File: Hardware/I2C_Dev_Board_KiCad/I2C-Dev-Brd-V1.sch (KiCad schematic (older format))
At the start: 23 parts, among them K1 POTS, P1 PICKIT2, P10 CONN_8, P2 FTDI SERIAL, P3 CONN_2, P4 CONN_6, P5 CONN_6, P6 CONN_4, P7 CONN_2, P8 CONN_2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

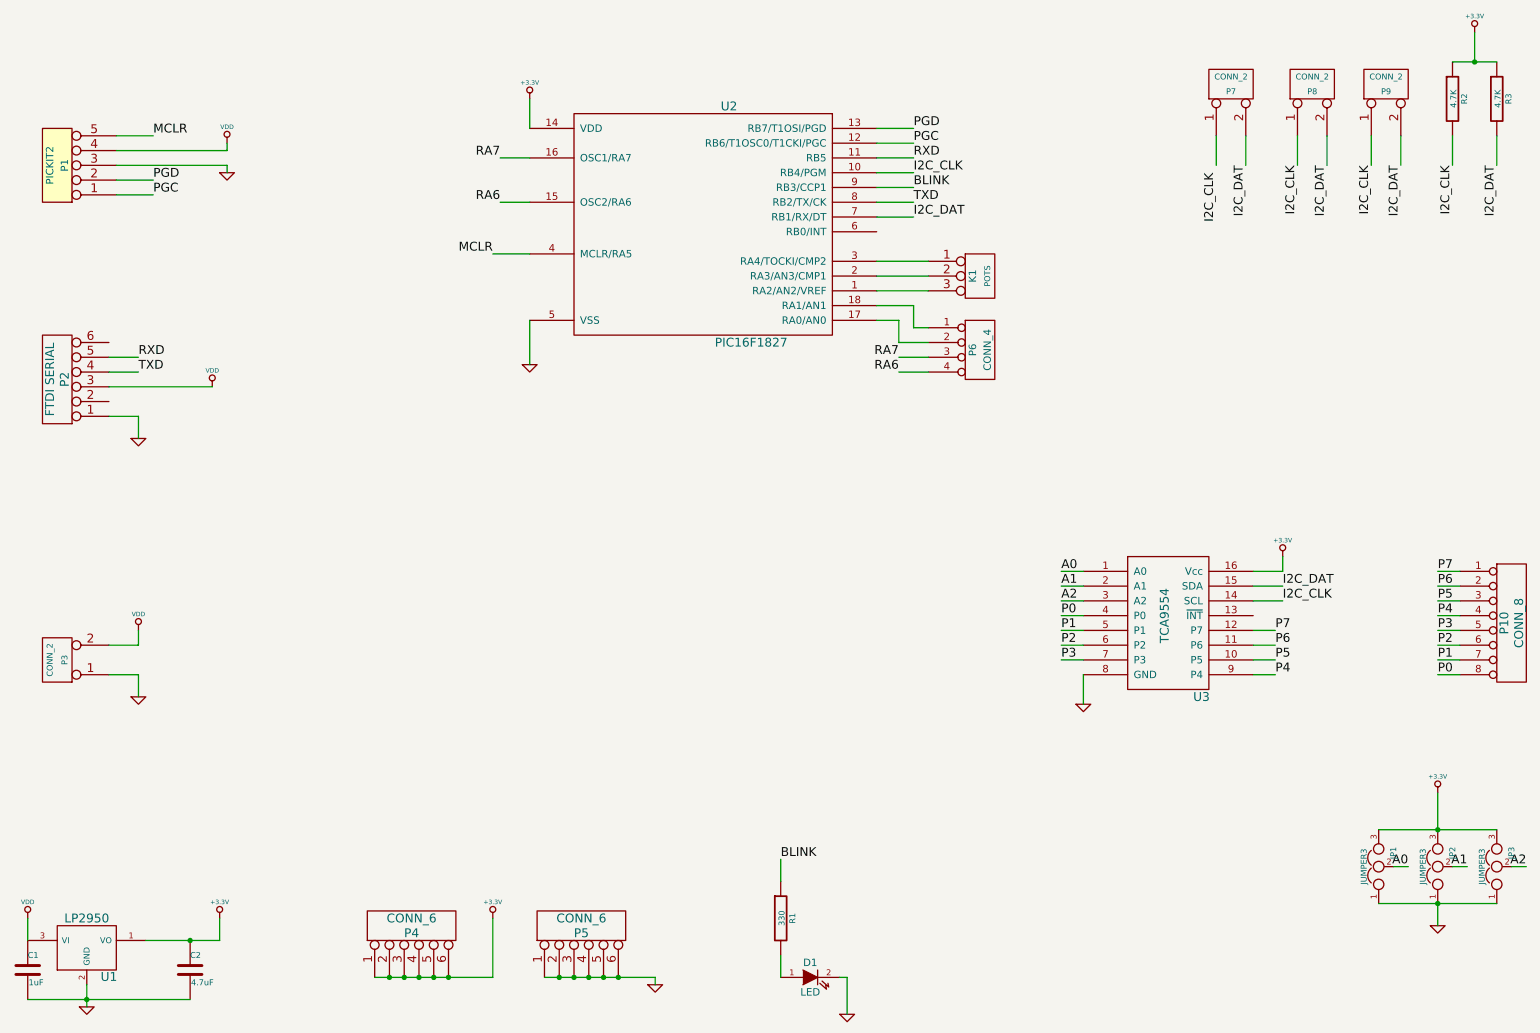
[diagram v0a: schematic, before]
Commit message: Added LUT table to firmware for VCO also added spreadsheet for LUT
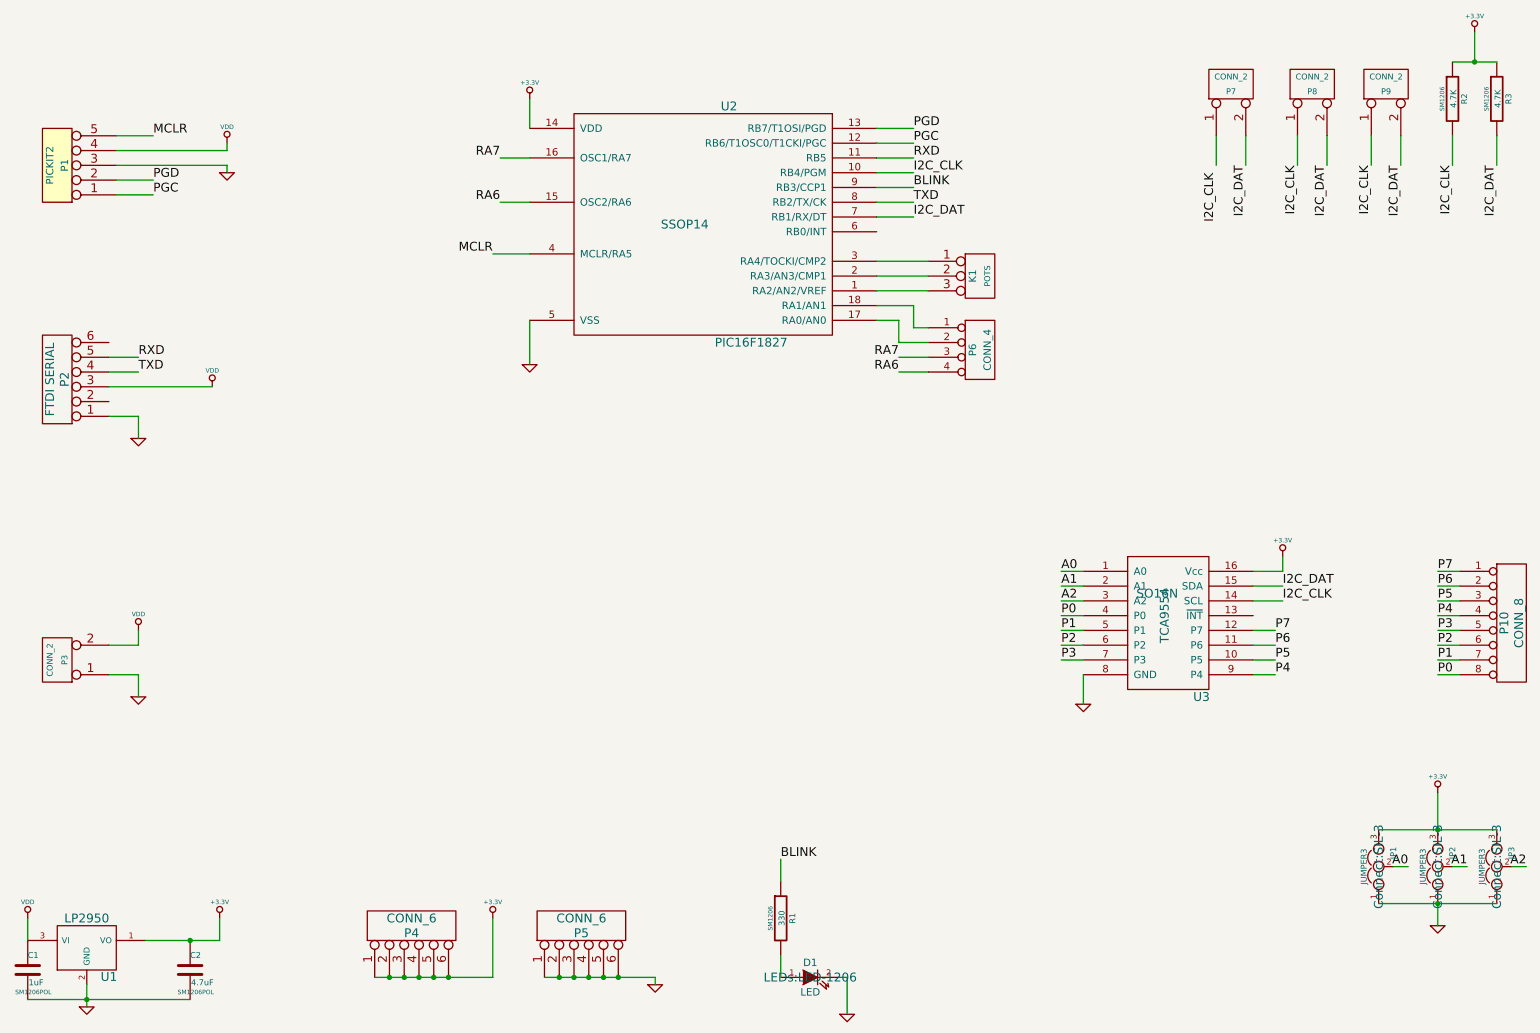
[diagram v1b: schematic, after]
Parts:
- C1, C2: footprint ~ -> SM1206POL
- D1: footprint ~ -> LEDs:LED-1206
- JP1, JP2, JP3: footprint ~ -> Connect:SIL-3
- K1: footprint (none) -> Connect:SIL-3
- P1: footprint (none) -> Connect:SIL-5
- P10: footprint (none) -> Connect:SIL-8
- P2, P4, P5: footprint (none) -> Connect:SIL-6
- P3, P7, P8, P9: footprint (none) -> Connect:SIL-2
- P6: footprint (none) -> Connect:SIL-4
- R1, R2, R3: footprint ~ -> SM1206
- U1: footprint (none) -> TO263
- U2: footprint ~ -> SSOP14
- U3: footprint ~ -> SO16N
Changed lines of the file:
@@
 LIBS:I2C
 LIBS:I2C-Dev-Brd-V1-cache
-EELAYER 27 0
+EELAYER 25 0
 EELAYER END
 $Descr A4 11693 8268
@@
 F 0 "U2" H 5600 2950 60  0000 C CNN
 F 1 "PIC16F1827" H 5750 1350 60  0000 C CNN
-F 2 "~" H 5300 2150 60  0000 C CNN
+F 2 "SSOP14" H 5300 2150 60  0000 C CNN
 F 3 "~" H 5300 2150 60  0000 C CNN
 	1    5300 2150
@@
 F 0 "P7" V 8950 1200 40  0000 C CNN
 F 1 "CONN_2" V 9050 1200 40  0000 C CNN
-F 2 "" H 9000 1200 60  0000 C CNN
+F 2 "Connect:SIL-2" H 9000 1200 60  0001 C CNN
 F 3 "" H 9000 1200 60  0000 C CNN
 	1    9000 1200
@@
 F 0 "P8" V 9500 1200 40  0000 C CNN
 F 1 "CONN_2" V 9600 1200 40  0000 C CNN
-F 2 "" H 9550 1200 60  0000 C CNN
+F 2 "Connect:SIL-2" H 9550 1200 60  0001 C CNN
 F 3 "" H 9550 1200 60  0000 C CNN
 	1    9550 1200
@@
 F 0 "P9" V 10000 1200 40  0000 C CNN
 F 1 "CONN_2" V 10100 1200 40  0000 C CNN
-F 2 "" H 10050 1200 60  0000 C CNN
+F 2 "Connect:SIL-2" H 10050 1200 60  0001 C CNN
 F 3 "" H 10050 1200 60  0000 C CNN
 	1    10050 1200
@@
 F 0 "R2" V 10580 1300 40  0000 C CNN
 F 1 "4.7K" V 10507 1301 40  0000 C CNN
-F 2 "~" V 10430 1300 30  0000 C CNN
+F 2 "SM1206" V 10430 1300 30  0000 C CNN
 F 3 "~" H 10500 1300 30  0000 C CNN
 	1    10500 1300
@@
 F 0 "R3" V 10880 1300 40  0000 C CNN
 F 1 "4.7K" V 10807 1301 40  0000 C CNN
-F 2 "~" V 10730 1300 30  0000 C CNN
+F 2 "SM1206" V 10730 1300 30  0000 C CNN
 F 3 "~" H 10800 1300 30  0000 C CNN
 	1    10800 1300
@@
 F 0 "P2" V 1000 3200 60  0000 C CNN
 F 1 "FTDI SERIAL" V 1100 3200 60  0000 C CNN
-F 2 "" H 1050 3200 60  0000 C CNN
+F 2 "Connect:SIL-6" H 1050 3200 60  0001 C CNN
 F 3 "" H 1050 3200 60  0000 C CNN
 	1    1050 3200
@@
 F 0 "D1" H 6150 7350 50  0000 C CNN
 F 1 "LED" H 6150 7150 50  0000 C CNN
-F 2 "~" H 6150 7250 60  0000 C CNN
+F 2 "LEDs:LED-1206" H 6150 7250 60  0000 C CNN
 F 3 "~" H 6150 7250 60  0000 C CNN
 	1    6150 7250
@@
 F 0 "R1" V 6030 6850 40  0000 C CNN
 F 1 "330" V 5957 6851 40  0000 C CNN
-F 2 "~" V 5880 6850 30  0000 C CNN
+F 2 "SM1206" V 5880 6850 30  0000 C CNN
 F 3 "~" H 5950 6850 30  0000 C CNN
 	1    5950 6850
@@
 F 0 "U1" H 1400 6854 60  0000 C CNN
 F 1 "LP2950" H 1250 7250 60  0000 C CNN
-F 2 "" H 1250 7050 60  0000 C CNN
+F 2 "TO263" H 1250 7050 60  0001 C CNN
 F 3 "" H 1250 7050 60  0000 C CNN
 	1    1250 7050
@@
 F 0 "C2" H 1950 7300 40  0000 L CNN
 F 1 "4.7uF" H 1956 7115 40  0000 L CNN
-F 2 "~" H 1988 7050 30  0000 C CNN
+F 2 "SM1206POL" H 1988 7050 30  0000 C CNN
 F 3 "~" H 1950 7200 60  0000 C CNN
 	1    1950 7200
@@
 F 0 "P1" V 1000 1750 50  0000 C CNN
 F 1 "PICKIT2" V 1100 1750 50  0000 C CNN
-F 2 "" H 1050 1750 60  0000 C CNN
+F 2 "Connect:SIL-5" H 1050 1750 60  0001 C CNN
 F 3 "" H 1050 1750 60  0000 C CNN
 	1    1050 1750
@@
 F 0 "P3" V 1000 5100 40  0000 C CNN
 F 1 "CONN_2" V 1100 5100 40  0000 C CNN
-F 2 "" H 1050 5100 60  0000 C CNN
+F 2 "Connect:SIL-2" H 1050 5100 60  0001 C CNN
 F 3 "" H 1050 5100 60  0000 C CNN
 	1    1050 5100
@@
 F 0 "K1" V 7250 2500 50  0000 C CNN
 F 1 "POTS" V 7350 2500 40  0000 C CNN
-F 2 "" H 7300 2500 60  0000 C CNN
+F 2 "Connect:SIL-3" H 7300 2500 60  0001 C CNN
 F 3 "" H 7300 2500 60  0000 C CNN
 	1    7300 2500
@@
 F 0 "P4" V 3400 6900 60  0000 C CNN
 F 1 "CONN_6" V 3500 6900 60  0000 C CNN
-F 2 "" H 3450 6900 60  0000 C CNN
+F 2 "Connect:SIL-6" H 3450 6900 60  0001 C CNN
 F 3 "" H 3450 6900 60  0000 C CNN
 	1    3450 6900
@@
 F 0 "P5" V 4550 6900 60  0000 C CNN
 F 1 "CONN_6" V 4650 6900 60  0000 C CNN
-F 2 "" H 4600 6900 60  0000 C CNN
+F 2 "Connect:SIL-6" H 4600 6900 60  0001 C CNN
 F 3 "" H 4600 6900 60  0000 C CNN
 	1    4600 6900
@@
 F 0 "P6" V 7250 3000 50  0000 C CNN
 F 1 "CONN_4" V 7350 3000 50  0000 C CNN
-F 2 "" H 7300 3000 60  0000 C CNN
+F 2 "Connect:SIL-4" H 7300 3000 60  0001 C CNN
 F 3 "" H 7300 3000 60  0000 C CNN
 	1    7300 3000
@@
 F 0 "U3" H 8800 4350 60  0000 C CNN
 F 1 "TCA9554" V 8550 4900 60  0000 C CNN
-F 2 "~" H 8500 5050 60  0000 C CNN
+F 2 "SO16N" H 8500 5050 60  0000 C CNN
 F 3 "~" H 8500 5050 60  0000 C CNN
 	1    8600 4850
@@
 F 0 "JP3" H 10850 6400 40  0000 L CNN
 F 1 "JUMPER3" H 10800 6600 40  0000 C CNN
-F 2 "~" H 10800 6500 60  0000 C CNN
+F 2 "Connect:SIL-3" H 10800 6500 60  0000 C CNN
 F 3 "~" H 10800 6500 60  0000 C CNN
 	1    10800 6500
@@
 F 0 "JP2" H 10450 6400 40  0000 L CNN
 F 1 "JUMPER3" H 10400 6600 40  0000 C CNN
-F 2 "~" H 10400 6500 60  0000 C CNN
+F 2 "Connect:SIL-3" H 10400 6500 60  0000 C CNN
 F 3 "~" H 10400 6500 60  0000 C CNN
 	1    10400 6500
@@
 F 0 "JP1" H 10050 6400 40  0000 L CNN
 F 1 "JUMPER3" H 10000 6600 40  0000 C CNN
-F 2 "~" H 10000 6500 60  0000 C CNN
+F 2 "Connect:SIL-3" H 10000 6500 60  0000 C CNN
 F 3 "~" H 10000 6500 60  0000 C CNN
 	1    10000 6500
@@
 F 0 "P10" V 10850 4850 60  0000 C CNN
 F 1 "CONN_8" V 10950 4850 60  0000 C CNN
-F 2 "" H 10900 4850 60  0000 C CNN
+F 2 "Connect:SIL-8" H 10900 4850 60  0001 C CNN
 F 3 "" H 10900 4850 60  0000 C CNN
 	1    10900 4850
@@
 F 0 "C1" H 850 7300 40  0000 L CNN
 F 1 "1uF" H 856 7115 40  0000 L CNN
-F 2 "~" H 888 7050 30  0000 C CNN
+F 2 "SM1206POL" H 888 7050 30  0000 C CNN
 F 3 "~" H 850 7200 60  0000 C CNN
 	1    850  7200
